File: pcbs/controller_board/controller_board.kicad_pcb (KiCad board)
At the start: 2 copper layers, 72 x 44 mm, 36 parts, among them J1 A-2014-2-4-N-T-R, J2 PINHD-1X7, J3 PINHD-1X12, J4 PINHD-1X4, P1 PJ-064A, U1 R-78E5.0-1.0, U2 PHOTON2, U3 BSS138, U4 BSS138, U5 BSS138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

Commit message: update controller board to version 0.73
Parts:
- D1: value SS36 -> 3A/60V/750mV; footprint footprints:D_SS36 -> footprints:D_DO-214AB_SMC
- D2: value SS36 -> 1A/40V/500mV; footprint footprints:D_SS36 -> footprints:D_DO-214AC_SMA
- D3: value SMBJ36A -> 40V; footprint footprints:TVS_SMBJ36A -> footprints:D_DO-214AA_SMB
- F1: value PFSM.075.2 -> 33V/750mA/1.5A; footprint footprints:POLYFUSE_SMD075F-2 -> footprints:Fuse_1812
- J1: value A-2014-2-4-N-T-R -> RJ45; footprint footprints:ASSMANN_A-2014-2-4-N-T-R -> footprints:RJ45_A-2014-2-4-N-T-R
- P1: value PJ-064A -> 24V / 5A
- Q1: renamed from U3; value BSS138 -> 220mA / 50V
- Q2: renamed from U4; value BSS138 -> 220mA / 50V
- Q3: renamed from U5; value BSS138 -> 220mA / 50V
- Q4: renamed from U6; value BSS138 -> 220mA / 50V
- R1, R10, R11, R12, R13, R14, R2, R3, R4, R5, R6, R8, R9: footprint footprints:R_1206_3216Metric_Pad1.30x1.75mm_HandSolder -> footprints:R_1206
- U1: value R-78E5.0-1.0 -> 8-28V in / 5V 5W out
- U2: value PHOTON2 -> Particle2 / Boron
- moved F1 1.25 mm to (107.0, 94.2), turned to 180 degrees
- moved R1 0.30 mm to (114.7, 117.5)
- moved R2 0.25 mm to (120.0, 117.5), turned to 0 degrees
- moved D1 0.22 mm to (119.0, 94.3)
- turned R10 to 90 degrees
- turned R12 to 90 degrees
- turned R13 to 90 degrees
- turned R14 to 90 degrees
- turned R8 to -90 degrees
- turned R9 to -90 degrees
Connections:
- F1 pad 1: Net-(F1-Pad1) -> Net-(D1-A)
- F1 pad 2: Net-(D1-A) -> Net-(F1-Pad2)
- P1 pad 1: Net-(F1-Pad1) -> Net-(F1-Pad2)
- Q1 pad 3: Net-(U3-D) -> Net-(Q1-D)
- R10 pad 1: +3V3 -> /D6-DECO
- R10 pad 2: /D6-DECO -> +3V3
- R12 pad 1: +3V3 -> /D1-SCL
- R12 pad 2: /D1-SCL -> +3V3
- R13 pad 1: /5V-SDA -> +5V
- R13 pad 2: +5V -> /5V-SDA
- R14 pad 1: +3V3 -> /D0-SDA
- R14 pad 2: /D0-SDA -> +3V3
- R2 pad 1: /A0-VIN -> GND
- R2 pad 2: GND -> /A0-VIN
- R8 pad 1: Net-(U3-D) -> +5V
- R8 pad 2: +5V -> Net-(Q1-D)
- R9 pad 1: /5V-DECO -> +5V
- R9 pad 2: +5V -> /5V-DECO
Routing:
- net Net-(F1-Pad1): track 20.2 -> 0.00 mm
- net Net-(F1-Pad2): track 0.00 -> 18.8 mm
- net Net-(U3-D): track 6.14 -> 0.00 mm
- net Net-(Q1-D): track 0.00 -> 6.14 mm
- net /VUSB: track 21.7 -> 25.0 mm
- net Net-(D1-A): track 3.42 -> 6.48 mm
- net /A0-VIN: track 21.5 -> 22.4 mm
- net +5V: track 188.8 -> 188.2 mm
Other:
- board text added: "Photon2 / Boron"
- board text removed: "U2 Photon2/Argon/Boron"

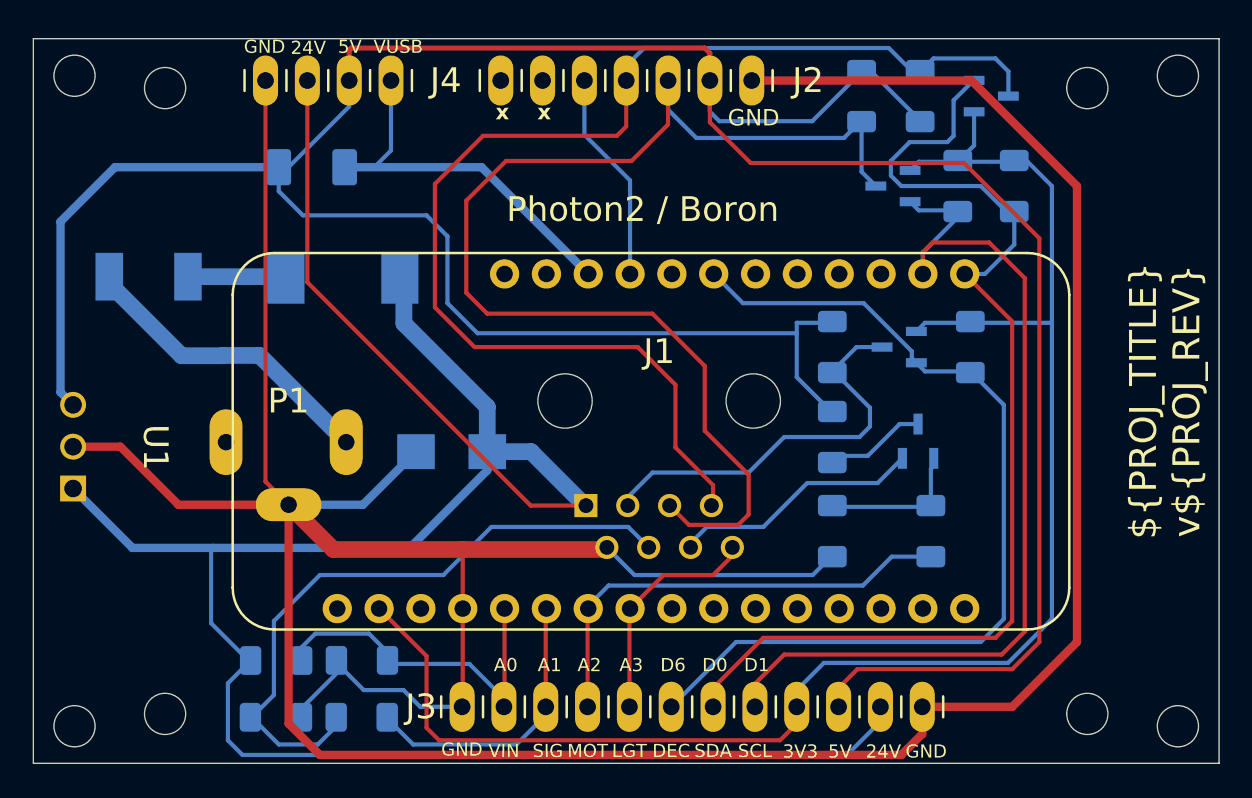
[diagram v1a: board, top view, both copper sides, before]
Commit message: update controller board to v0.80
- switch 5V rail to go to device (instead of light output)
- improve protection of 3V/5V I2C bus by using an IC instead of mosfets
- bleed resistor from external 5V to gnd to avoid floating voltage
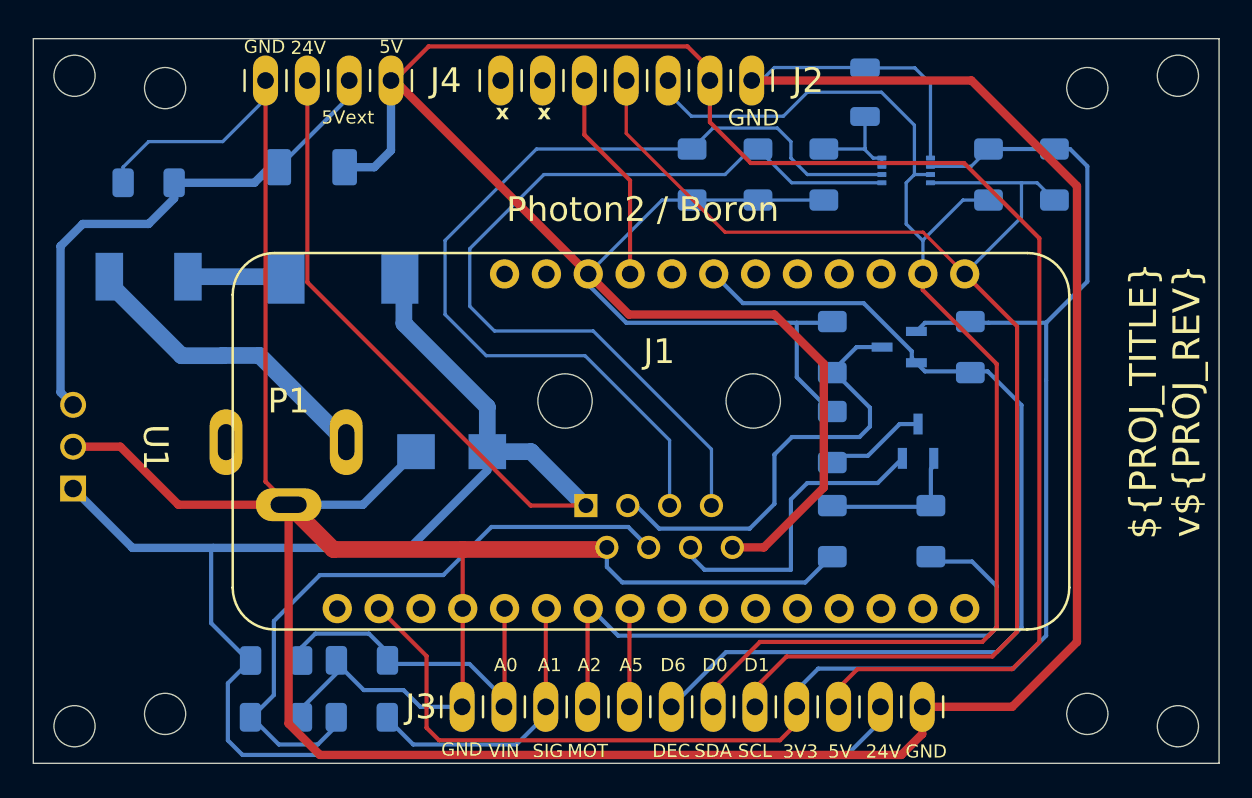
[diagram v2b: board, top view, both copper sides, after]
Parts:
- removed Q3, Q4: 220mA / 50V, footprints:SOT-23-3
- added C1: 100pF, footprints:C_1206, B.Cu at (150.5, 83.0)
- added R15: 200kΩ, footprints:R_1206, B.Cu at (148.0, 88.0)
- added R7: 10kΩ, footprints:R_1206, B.Cu at (107.0, 88.5)
- added U3: A: 1.2 to 3.3V B: 1.8 to 5.5V, footprints:SOT-765-1_VSSOP8, B.Cu at (153.0, 87.8)
- R11, R12, R13, R14: value 10kΩ -> 2.2kΩ
- moved R14 15.6 mm to (144.0, 88.0), turned to -90 degrees
- moved R13 14.6 mm to (140.0, 88.0), turned to -90 degrees
- moved R11 12.6 mm to (162.0, 88.0)
- moved R12 1.99 mm to (158.0, 88.0)
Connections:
- D2 pad 1: /VUSB -> +5V
- D2 pad 2: +5V -> /Vout
- J1 pad 8: /A3-LIGHT -> +5V
- J2 pad 3: /5V-SCL -> /D1-SCL
- J2 pad 4: /5V-SDA -> /D0-SDA
- J3 pad 5: /A3-LIGHT -> /A5
- J3 pad 7: /D0-SDA -> /D1-SCL
- J3 pad 8: /D1-SCL -> /D0-SDA
- J4 pad 3: +5V -> /Vout
- J4 pad 4: /VUSB -> +5V
- R11 pad 1: /5V-SCL -> /D0-SDA
- R11 pad 2: +5V -> +3V3
- R13 pad 1: +5V -> /5V-SCL
- R13 pad 2: /5V-SDA -> +5V
- R14 pad 1: /D0-SDA -> /5V-SDA
- R14 pad 2: +3V3 -> +5V
- U1 pad 3: +5V -> /Vout
- U2 pad 26: /VUSB -> +5V
- U2 pad 8: /A3-LIGHT -> /A5
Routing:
- net /Vout: track 0.00 -> 32.8 mm
- net GND: track 223.6 -> 253.5 mm
- net /VUSB: track 25.0 -> 0.00 mm
- net /5V-SDA: track 75.5 -> 53.7 mm
- net /D1-SCL: track 57.0 -> 77.7 mm
- net /D0-SDA: track 66.7 -> 86.0 mm
- net /5V-SCL: track 73.4 -> 56.4 mm
- net /A3-LIGHT: track 14.0 -> 0.00 mm
- net /A2-MOTOR: track 28.2 -> 39.2 mm
- net +5V: track 188.2 -> 180.9 mm
- net Net-(U3-EN): track 0.00 -> 6.25 mm
- net /A5: track 0.00 -> 5.98 mm
- net /5V-SPEED: track 15.3 -> 19.0 mm
- net /5V-DECO: track 25.0 -> 27.6 mm
- net /D6-DECO: track 56.6 -> 59.0 mm
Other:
- board text added: "5Vext"
- board text added: "A5"
- board text removed: "A3"
- board text removed: "LGT"
- board text removed: "VUSB"

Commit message: v 0.81 (removed the 5V on the RJ45)
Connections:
- J1 pad 8: +5V -> unconnected-(J1-Pad8)
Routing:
- net +5V: track 180.9 -> 149.2 mm
- net unconnected-(J1-Pad8): track 0.00 -> 0.51 mm
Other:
- board text added: "5V (ext)"
- board text removed: "5Vext"
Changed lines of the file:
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@@
 	)
 	(property "PROJ_AUTHOR" "Sebastian Kopf")
-	(property "PROJ_REV" "0.80")
+	(property "PROJ_REV" "0.81")
 	(property "PROJ_TITLE" "µLogger Controller Board")
 	(net 0 "")
@@
 	(net 42 "unconnected-(P1-Pad3)")
 	(net 43 "/A5")
+	(net 44 "unconnected-(J1-Pad8)")
 	(footprint "footprints:MountingHole_2.5mm_M2.5"
 		(layer "F.Cu")
@@
 			(layers "*.Cu" "*.Mask")
 			(remove_unused_layers no)
-			(net 18 "+5V")
+			(net 44 "unconnected-(J1-Pad8)")
 			(pinfunction "8")
-			(pintype "passive")
+			(pintype "passive+no_connect")
 			(solder_mask_margin 0.1016)
 			(thermal_bridge_angle 0)
@@
 		)
 	)
-	(gr_text "5Vext"
-		(at 117.5 85 0)
+	(gr_text "5V\n(ext)"
+		(at 119.184247 84.547536 0)
 		(layer "F.SilkS")
 		(effects
@@
 				(thickness 0.08)
 			)
-			(justify left bottom)
+			(justify top)
 		)
 	)
@@
 	)
 	(gr_text "GND"
-		(at 112.781621 80.70934 0)
+		(at 114.097 84.505435 0)
 		(layer "F.SilkS")
 		(effects
@@
 				(thickness 0.08)
 			)
-			(justify left bottom)
+			(justify top)
 		)
 	)
@@
 	)
 	(gr_text "24V"
-		(at 115.62338 80.77547 0)
+		(at 116.637 84.484385 0)
 		(layer "F.SilkS")
 		(effects
@@
 				(thickness 0.08)
 			)
-			(justify left bottom)
+			(justify top)
 		)
 	)
@@
 	)
 	(gr_text "5V"
-		(at 121 80.70934 0)
+		(at 121.64712 85.052741 0)
 		(layer "F.SilkS")
 		(effects
@@
 				(thickness 0.08)
 			)
-			(justify left bottom)
 		)
 	)
@@
 	)
 	(segment
-		(start 136.159 96.5)
-		(end 145 96.5)
-		(width 0.508)
-		(layer "F.Cu")
-		(net 18)
-	)
-	(segment
 		(start 121.937188 82.29)
 		(end 121.717 82.29)
@@
 	)
 	(segment
-		(start 133.694 94.035)
-		(end 136.159 96.5)
-		(width 0.508)
-		(layer "F.Cu")
-		(net 18)
-	)
-	(segment
 		(start 141.08 84.82)
 		(end 141.08 82.29)
@@
 	)
 	(segment
-		(start 148 107)
-		(end 144.36 110.64)
-		(width 0.508)
-		(layer "F.Cu")
-		(net 18)
-	)
-	(segment
 		(start 139.718686 80.218686)
 		(end 124 80.218686)
@@
 	)
 	(segment
-		(start 148 99.5)
-		(end 148 107)
-		(width 0.508)
-		(layer "F.Cu")
-		(net 18)
-	)
-	(segment
 		(start 124 80.218686)
 		(end 124 80.227188)
@@
 	)
 	(segment
-		(start 145 96.5)
-		(end 148 99.5)
-		(width 0.508)
-		(layer "F.Cu")
-		(net 18)
-	)
-	(segment
-		(start 144.36 110.64)
-		(end 142.445 110.64)
-		(width 0.508)
-		(layer "F.Cu")
-		(net 18)
-	)
-	(segment
 		(start 121.717 82.29)
 		(end 121.949 82.29)
@@
 	)
 	(segment
-		(start 142.445 111.15)
-		(end 142.445 110.64)
-		(width 0.254)
-		(layer "F.Cu")
-		(net 18)
-	)
-	(segment
 		(start 150.038 118.035)
 		(end 159.436 118.035)
@@
 		(net 43)
 	)
+	(segment
+		(start 142.445 111.15)
+		(end 142.445 110.64)
+		(width 0.254)
+		(layer "F.Cu")
+		(net 44)
+	)
 	(embedded_fonts no)

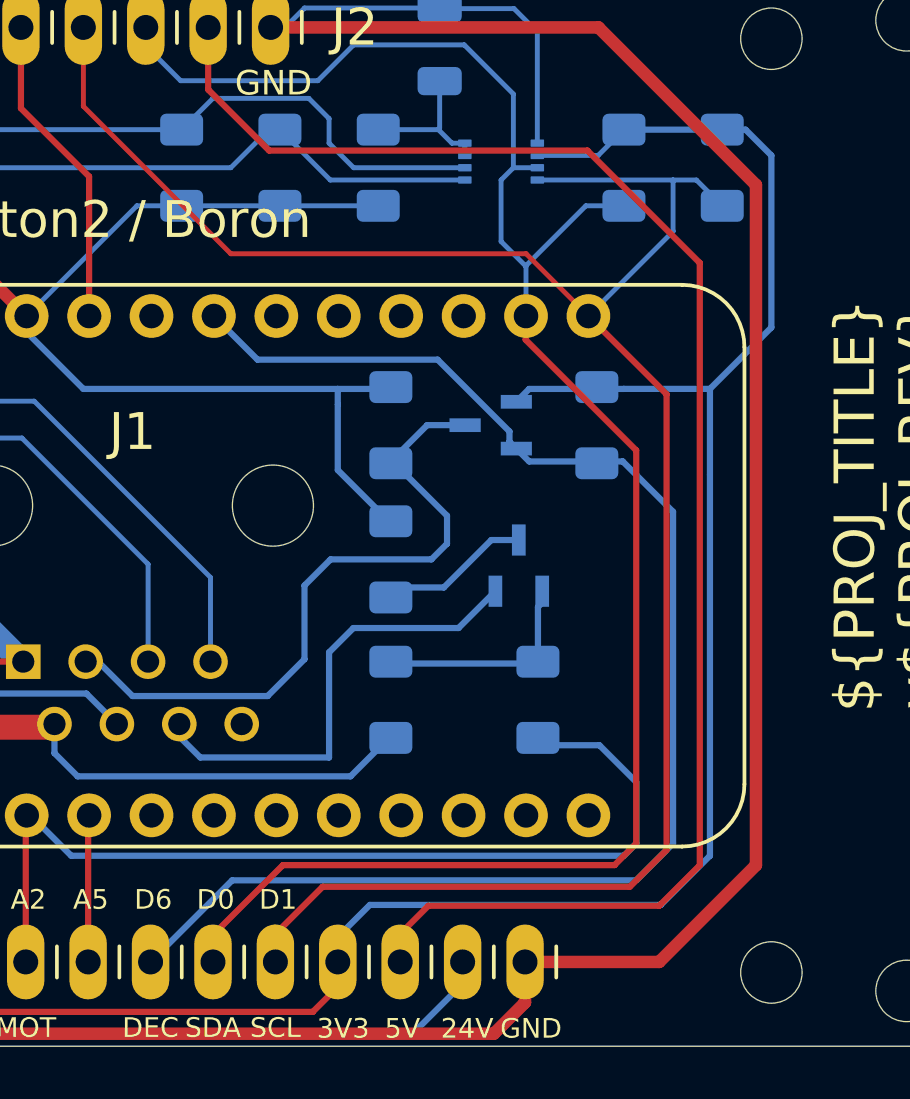
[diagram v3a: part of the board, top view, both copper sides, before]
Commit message: include board version information (version 1.0)
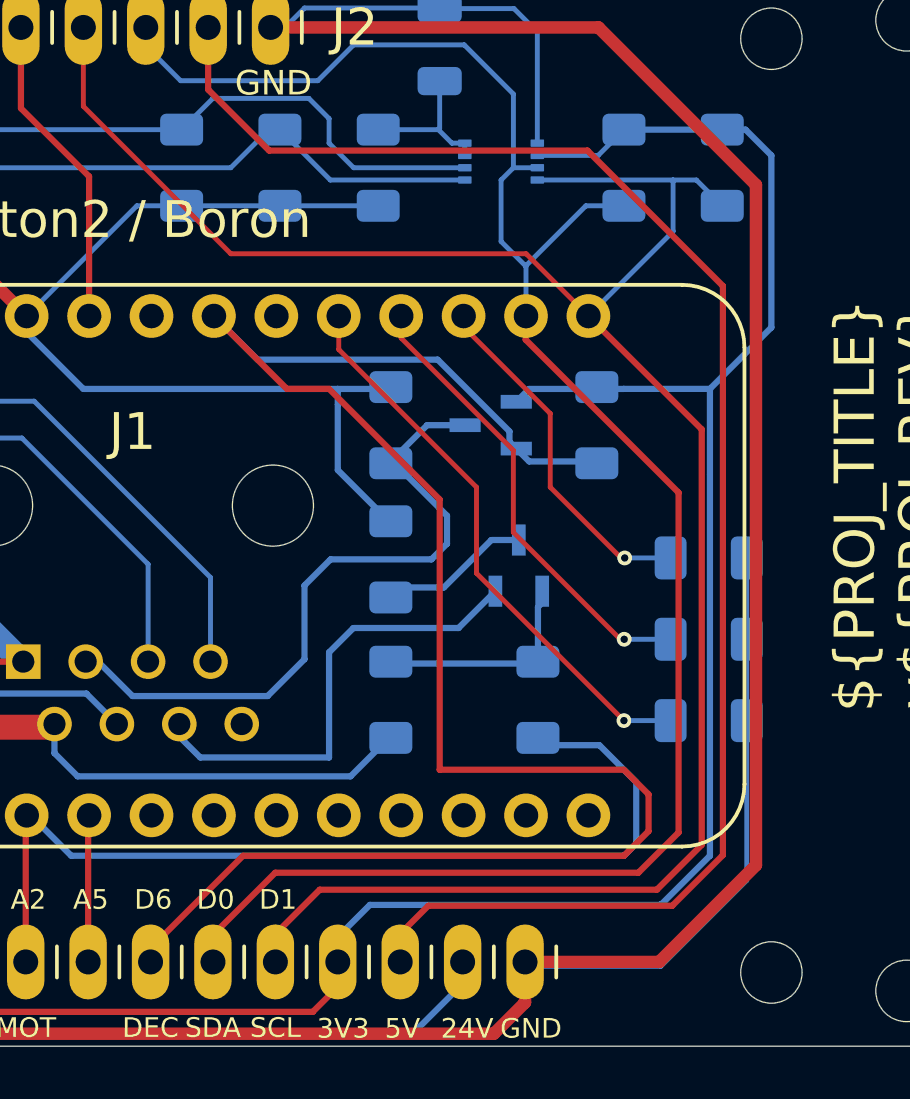
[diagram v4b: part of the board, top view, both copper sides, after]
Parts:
- added R16: 10kΩ, footprints:R_1206, B.Cu at (161.4, 103.9)
- added R17: 10kΩ, footprints:R_1206, B.Cu at (161.4, 107.2)
- added R18: 10kΩ, footprints:R_1206, B.Cu at (161.4, 110.5)
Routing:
- net GND: track 253.5 -> 277.2 mm
- net /D4: track 0.00 -> 23.2 mm, vias 0 -> 1
- net /D3: track 0.00 -> 18.9 mm, vias 0 -> 1
- net /D6-DECO: track 59.0 -> 74.8 mm
- net /D2: track 0.00 -> 14.5 mm, vias 0 -> 1
- net /D1-SCL: track 77.7 -> 79.9 mm
- net /D0-SDA: track 86.0 -> 87.9 mm
- net +5V: track 149.2 -> 150.3 mm
